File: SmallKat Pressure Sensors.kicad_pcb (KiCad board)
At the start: 2 copper layers, 20 x 20 mm, 7 parts, among them J1 Conn_01x04_Male, U1 LPS25HB

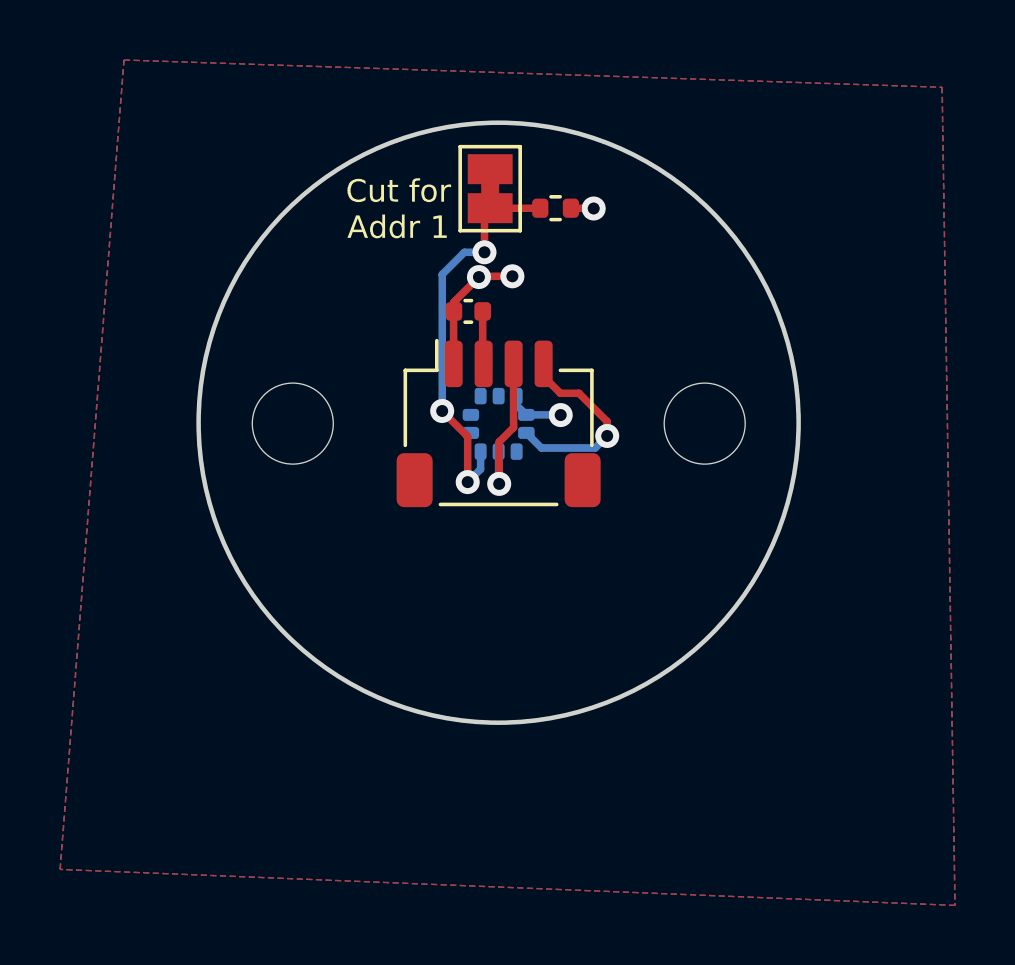
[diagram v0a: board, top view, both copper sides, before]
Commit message: updated to single sided assembly
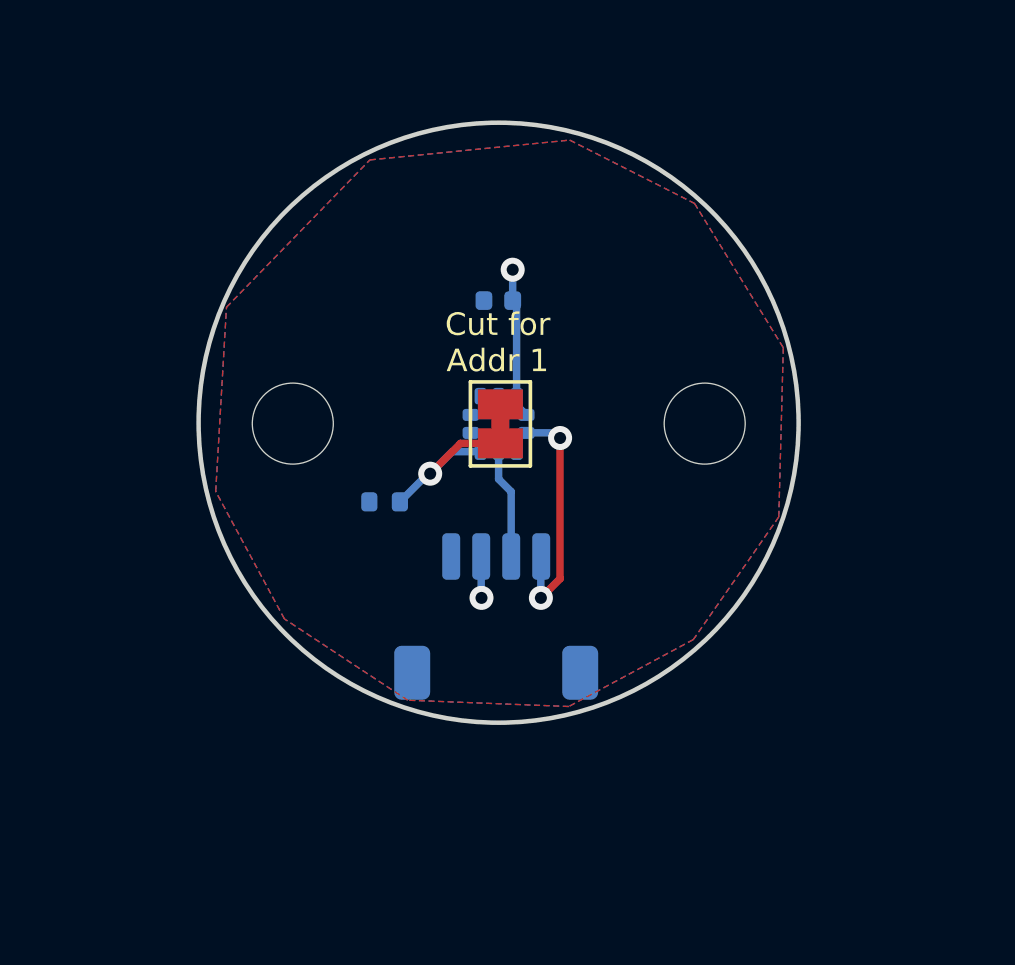
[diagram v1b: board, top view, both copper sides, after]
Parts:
- C1: value C -> 0.1uF; moved to B.Cu
- J1, R1: moved to B.Cu
- moved R1 11.3 mm to (26.3, 29.4), turned to 180 degrees
- moved JP1 7.85 mm to (30.2, 26.8)
- moved J1 6.42 mm to (30.0, 33.2), turned to 180 degrees
- moved C1 1.06 mm to (30.1, 22.6)
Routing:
- net Net-(JP1-Pad1): track 13.4 -> 6.14 mm, vias 3 -> 1
- net GND: track 5.13 -> 0.00 mm, vias 3 -> 0
- net +3V3: track 3.67 -> 6.41 mm, vias 1 -> 2
- net /SDA: track 5.28 -> 3.67 mm, vias 1 -> 0
- net /SCL: track 6.71 -> 8.17 mm, vias 1 -> 2
